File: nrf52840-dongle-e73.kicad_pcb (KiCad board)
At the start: 2 copper layers, 13.7 x 30 mm, 4 parts, among them J1 Conn_01x04_Female, J2 Conn_01x02_Female, J3 USB_A, U1 E73-2G4M08S1C-52840

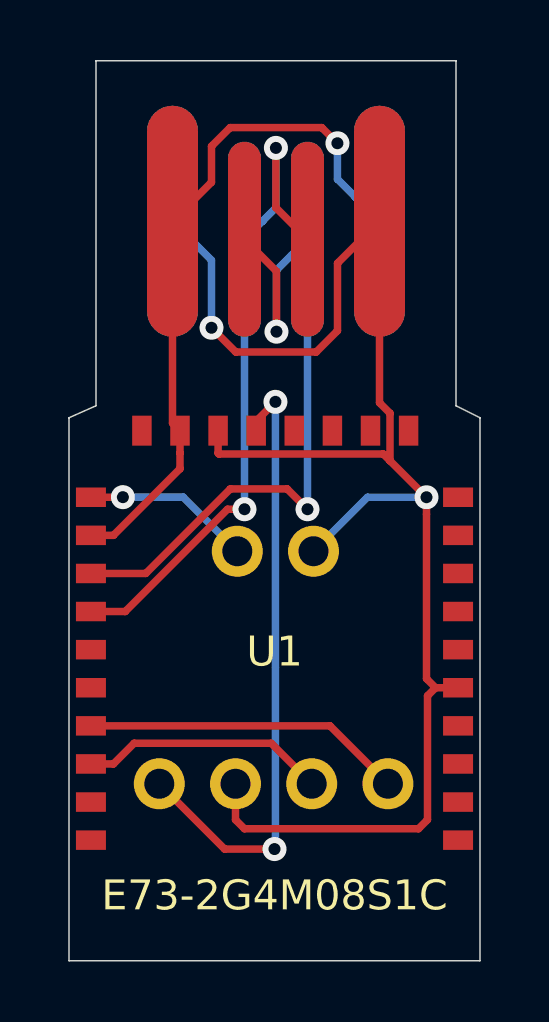
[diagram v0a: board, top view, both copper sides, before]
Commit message: Remove reversability
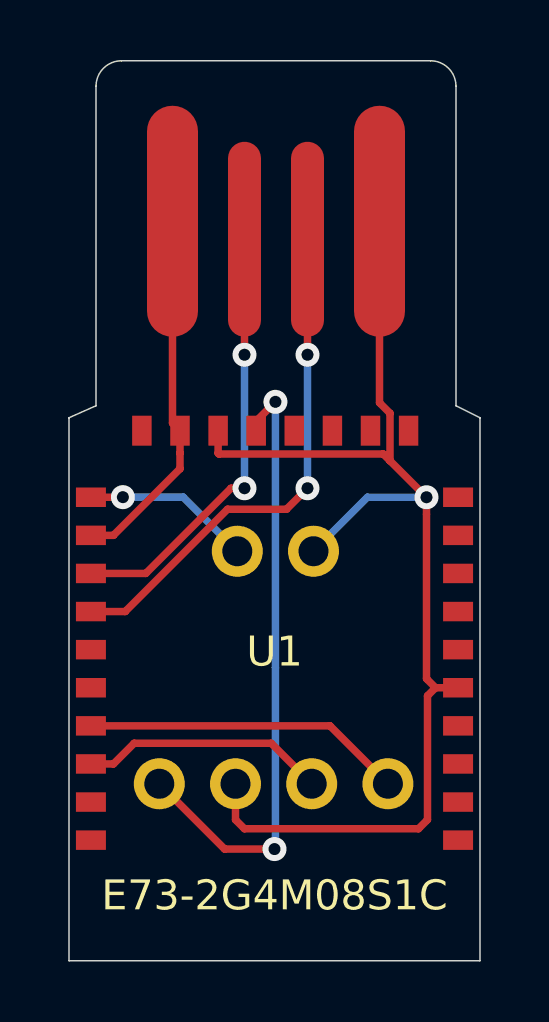
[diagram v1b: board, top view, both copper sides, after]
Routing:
- net GND: track 53.7 -> 40.5 mm, vias 2 -> 1
- net VBUS: track 23.1 -> 12.2 mm, vias 1 -> 0
- net Net-(J3-Pad2): track 24.7 -> 14.6 mm
- net Net-(J3-Pad3): track 22.5 -> 17.2 mm
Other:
- outline, holes or cut-outs redrawn
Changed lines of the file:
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@@
   (general
     (thickness 1.6)
-    (drawings 14)
-    (tracks 88)
+    (drawings 16)
+    (tracks 63)
     (zones 0)
     (modules 4)
@@
     (add_net VCC)
   )
+  (module nrf52840-dongle-e73:usb-pcb (layer F.Cu)
+    (at 53.55 49.9)
+    (fp_text reference J3 (at 0 4.65) (layer F.SilkS) hide
+      (effects (font (size 1 1) (thickness 0.15)))
+    )
+    (fp_text value USB_A (at 0 -4.55) (layer F.Fab)
+      (effects (font (size 1 1) (thickness 0.15)))
+    )
+    (fp_line (start -6 6.15) (end -6 -5.35) (layer F.Fab) (width 0.12))
+    (fp_line (start 6 6.15) (end -6 6.15) (layer F.Fab) (width 0.12))
+    (fp_line (start 6 -5.35) (end 6 6.15) (layer F.Fab) (width 0.12))
+    (fp_line (start -6 -5.35) (end 6 -5.35) (layer F.Fab) (width 0.12))
+    (pad 3 smd oval (at 1.05 0.6) (size 1.1 6.5) (layers F.Cu F.Paste F.Mask)
+      (net 6 "Net-(J3-Pad3)"))
+    (pad 2 smd oval (at -1.05 0.6) (size 1.1 6.5) (layers F.Cu F.Paste F.Mask)
+      (net 7 "Net-(J3-Pad2)"))
+    (pad 4 smd oval (at 3.45 0) (size 1.7 7.7) (layers F.Cu F.Paste F.Mask)
+      (net 2 GND))
+    (pad 1 smd oval (at -3.45 0) (size 1.7 7.7) (layers F.Cu F.Paste F.Mask)
+      (net 8 VBUS))
+  )
   (module nrfmicro:E73-2G4M08S1C-52840-NO-UNDER (layer F.Cu)
     (at 53.5 56.5 270)
@@
     )
   )
-  (module nrf52840-dongle-e73:usb-pcb (layer F.Cu)
-    (at 53.55 49.9)
-    (fp_text reference J3 (at 0 4.65) (layer F.SilkS) hide
-      (effects (font (size 1 1) (thickness 0.15)))
-    )
-    (fp_text value USB_A (at 0 -4.55) (layer F.Fab)
-      (effects (font (size 1 1) (thickness 0.15)))
-    )
-    (fp_line (start -6 6.15) (end -6 -5.35) (layer F.Fab) (width 0.12))
-    (fp_line (start 6 6.15) (end -6 6.15) (layer F.Fab) (width 0.12))
-    (fp_line (start 6 -5.35) (end 6 6.15) (layer F.Fab) (width 0.12))
-    (fp_line (start -6 -5.35) (end 6 -5.35) (layer F.Fab) (width 0.12))
-    (pad 3 smd oval (at -1.05 0.6) (size 1.1 6.5) (layers B.Cu B.Paste B.Mask)
-      (net 6 "Net-(J3-Pad3)"))
-    (pad 2 smd oval (at 1.05 0.6) (size 1.1 6.5) (layers B.Cu B.Paste B.Mask)
-      (net 7 "Net-(J3-Pad2)"))
-    (pad 4 smd oval (at -3.45 0) (size 1.7 7.7) (layers B.Cu B.Paste B.Mask)
-      (net 2 GND))
-    (pad 1 smd oval (at 3.45 0) (size 1.7 7.7) (layers B.Cu B.Paste B.Mask)
-      (net 8 VBUS))
-    (pad 3 smd oval (at 1.05 0.6) (size 1.1 6.5) (layers F.Cu F.Paste F.Mask)
-      (net 6 "Net-(J3-Pad3)"))
-    (pad 2 smd oval (at -1.05 0.6) (size 1.1 6.5) (layers F.Cu F.Paste F.Mask)
-      (net 7 "Net-(J3-Pad2)"))
-    (pad 4 smd oval (at 3.45 0) (size 1.7 7.7) (layers F.Cu F.Paste F.Mask)
-      (net 2 GND))
-    (pad 1 smd oval (at -3.45 0) (size 1.7 7.7) (layers F.Cu F.Paste F.Mask)
-      (net 8 VBUS))
-  )
   (module nrf52840-dongle-e73:reset-conn (layer F.Cu)
     (at 52.26 60.9 90)
@@
       (net 4 VCC))
   )
+  (gr_arc (start 58.7 45.4) (end 59.55 45.4) (angle -90) (layer Edge.Cuts) (width 0.05))
+  (gr_arc (start 48.4 45.4) (end 48.4 44.55) (angle -90) (layer Edge.Cuts) (width 0.05))
   (gr_text GND (at 54.8 63.6 270) (layer B.SilkS)
     (effects (font (size 1 1) (thickness 0.15)) (justify mirror))
@@
   (gr_line (start 46.65 56.45) (end 47.55 56.05) (layer Edge.Cuts) (width 0.05))
   (gr_line (start 46.65 74.55) (end 46.65 56.45) (layer Edge.Cuts) (width 0.05))
-  (gr_line (start 47.55 44.55) (end 47.55 56.05) (layer Edge.Cuts) (width 0.05))
-  (gr_line (start 59.55 44.55) (end 59.55 56.05) (layer Edge.Cuts) (width 0.05))
-  (gr_line (start 47.55 44.55) (end 59.55 44.55) (layer Edge.Cuts) (width 0.05))
+  (gr_line (start 47.55 45.4) (end 47.55 56.05) (layer Edge.Cuts) (width 0.05))
+  (gr_line (start 59.55 45.4) (end 59.55 56.05) (layer Edge.Cuts) (width 0.05))
+  (gr_line (start 48.4 44.55) (end 58.7 44.55) (layer Edge.Cuts) (width 0.05))
   (gr_text SWD (at 57.3 71.45 270) (layer B.SilkS)
     (effects (font (size 1 1) (thickness 0.15)) (justify mirror))
@@
   (segment (start 53.39 67.3) (end 54.74 68.65) (width 0.25) (layer F.Cu) (net 1))
   (segment (start 48.821 67.3) (end 53.39 67.3) (width 0.25) (layer F.Cu) (net 1))
-  (segment (start 50.1 49.9) (end 50.5 50.3) (width 0.25) (layer B.Cu) (net 2))
-  (via (at 51.4 53.45) (size 0.8) (drill 0.4) (layers F.Cu B.Cu) (net 2))
-  (segment (start 50.5 50.3) (end 51.4 51.2) (width 0.25) (layer B.Cu) (net 2))
-  (segment (start 51.4 51.2) (end 51.4 53.45) (width 0.25) (layer B.Cu) (net 2))
-  (segment (start 55.6 53.55) (end 54.891494 54.258506) (width 0.25) (layer F.Cu) (net 2))
-  (segment (start 52.208506 54.258506) (end 51.4 53.45) (width 0.25) (layer F.Cu) (net 2))
-  (segment (start 57 49.9) (end 55.6 51.3) (width 0.25) (layer F.Cu) (net 2))
-  (segment (start 54.891494 54.258506) (end 52.208506 54.258506) (width 0.25) (layer F.Cu) (net 2))
-  (segment (start 55.6 51.3) (end 55.6 53.55) (width 0.25) (layer F.Cu) (net 2))
   (segment (start 51.62 57.631) (end 51.62 56.881) (width 0.25) (layer F.Cu) (net 2))
   (segment (start 51.647401 57.658401) (end 51.62 57.631) (width 0.25) (layer F.Cu) (net 2))
@@
   (segment (start 50.456505 59.096505) (end 52.26 60.9) (width 0.25) (layer B.Cu) (net 5))
   (segment (start 48.446505 59.096505) (end 50.456505 59.096505) (width 0.25) (layer B.Cu) (net 5))
-  (segment (start 52.5 50.5) (end 53.1 49.9) (width 0.25) (layer B.Cu) (net 6))
-  (via (at 53.547141 47.455351) (size 0.8) (drill 0.4) (layers F.Cu B.Cu) (net 6))
-  (segment (start 53.1 49.9) (end 53.547141 49.452859) (width 0.25) (layer B.Cu) (net 6))
-  (segment (start 53.547141 49.452859) (end 53.547141 47.455351) (width 0.25) (layer B.Cu) (net 6))
-  (segment (start 53.547141 47.455351) (end 53.547141 49.447141) (width 0.25) (layer F.Cu) (net 6))
-  (segment (start 53.547141 49.447141) (end 54.6 50.5) (width 0.25) (layer F.Cu) (net 6))
-  (via (at 52.5 59.5) (size 0.8) (drill 0.4) (layers F.Cu B.Cu) (net 6))
-  (segment (start 52.5 50.5) (end 52.5 59.5) (width 0.25) (layer B.Cu) (net 6))
   (segment (start 48.524315 62.91) (end 47.381 62.91) (width 0.25) (layer F.Cu) (net 6))
-  (segment (start 52.5 59.5) (end 51.934315 59.5) (width 0.25) (layer F.Cu) (net 6))
   (segment (start 51.934315 59.5) (end 48.524315 62.91) (width 0.25) (layer F.Cu) (net 6))
-  (segment (start 54.6 50.5) (end 54.05 51.05) (width 0.25) (layer B.Cu) (net 7))
-  (segment (start 54.05 51.05) (end 53.56557 51.53443) (width 0.25) (layer B.Cu) (net 7))
-  (via (at 53.56557 53.581105) (size 0.8) (drill 0.4) (layers F.Cu B.Cu) (net 7))
-  (segment (start 53.56557 51.53443) (end 53.56557 53.581105) (width 0.25) (layer B.Cu) (net 7))
-  (segment (start 53.56557 51.56557) (end 53.56557 53.581105) (width 0.25) (layer F.Cu) (net 7))
-  (segment (start 52.5 50.5) (end 53.56557 51.56557) (width 0.25) (layer F.Cu) (net 7))
-  (via (at 54.6 59.5) (size 0.8) (drill 0.4) (layers F.Cu B.Cu) (net 7))
-  (segment (start 54.6 50.5) (end 54.6 59.5) (width 0.25) (layer B.Cu) (net 7))
-  (segment (start 53.922599 58.822599) (end 52.027401 58.822599) (width 0.25) (layer F.Cu) (net 7))
-  (segment (start 54.6 59.5) (end 53.922599 58.822599) (width 0.25) (layer F.Cu) (net 7))
+  (via (at 54.6 54.35) (size 0.8) (drill 0.4) (layers F.Cu B.Cu) (net 6))
+  (segment (start 54.6 50.5) (end 54.6 54) (width 0.25) (layer F.Cu) (net 6))
+  (segment (start 54.6 54) (end 54.6 54.35) (width 0.25) (layer F.Cu) (net 6))
+  (via (at 54.6 58.8) (size 0.8) (drill 0.4) (layers F.Cu B.Cu) (net 6))
+  (segment (start 54.6 54.35) (end 54.6 58.8) (width 0.25) (layer B.Cu) (net 6))
+  (segment (start 53.9 59.5) (end 51.934315 59.5) (width 0.25) (layer F.Cu) (net 6))
+  (segment (start 54.6 58.8) (end 53.9 59.5) (width 0.25) (layer F.Cu) (net 6))
+  (via (at 52.5 54.35) (size 0.8) (drill 0.4) (layers F.Cu B.Cu) (net 7))
+  (segment (start 52.5 50.5) (end 52.5 54.35) (width 0.25) (layer F.Cu) (net 7))
+  (via (at 52.5 58.8) (size 0.8) (drill 0.4) (layers F.Cu B.Cu) (net 7))
+  (segment (start 52.5 54.35) (end 52.5 58.8) (width 0.25) (layer B.Cu) (net 7))
   (segment (start 49.21 61.64) (end 47.381 61.64) (width 0.25) (layer F.Cu) (net 7))
-  (segment (start 52.027401 58.822599) (end 49.21 61.64) (width 0.25) (layer F.Cu) (net 7))
-  (segment (start 57 49.9) (end 56.2 49.1) (width 0.25) (layer B.Cu) (net 8))
-  (via (at 55.5976 47.3) (size 0.8) (drill 0.4) (layers F.Cu B.Cu) (net 8))
-  (segment (start 56.2 49.1) (end 55.5976 48.4976) (width 0.25) (layer B.Cu) (net 8))
-  (segment (start 55.5976 48.4976) (end 55.5976 47.3) (width 0.25) (layer B.Cu) (net 8))
-  (segment (start 55.07555 46.77795) (end 55.5976 47.3) (width 0.25) (layer F.Cu) (net 8))
-  (segment (start 51.4 47.4) (end 52.02205 46.77795) (width 0.25) (layer F.Cu) (net 8))
-  (segment (start 52.02205 46.77795) (end 55.07555 46.77795) (width 0.25) (layer F.Cu) (net 8))
-  (segment (start 50.1 49.9) (end 51.4 48.6) (width 0.25) (layer F.Cu) (net 8))
-  (segment (start 51.4 48.6) (end 51.4 47.4) (width 0.25) (layer F.Cu) (net 8))
+  (segment (start 52.5 58.8) (end 52.05 58.8) (width 0.25) (layer F.Cu) (net 7))
+  (segment (start 52.05 58.8) (end 49.21 61.64) (width 0.25) (layer F.Cu) (net 7))
   (segment (start 50.1 56.631) (end 50.35 56.881) (width 0.25) (layer F.Cu) (net 8))
   (segment (start 50.1 49.9) (end 50.1 56.631) (width 0.25) (layer F.Cu) (net 8))
